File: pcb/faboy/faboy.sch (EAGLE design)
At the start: 51 parts, among them U1 MAX1595UMAX, U2 MCP73831, Y1 16MHZ

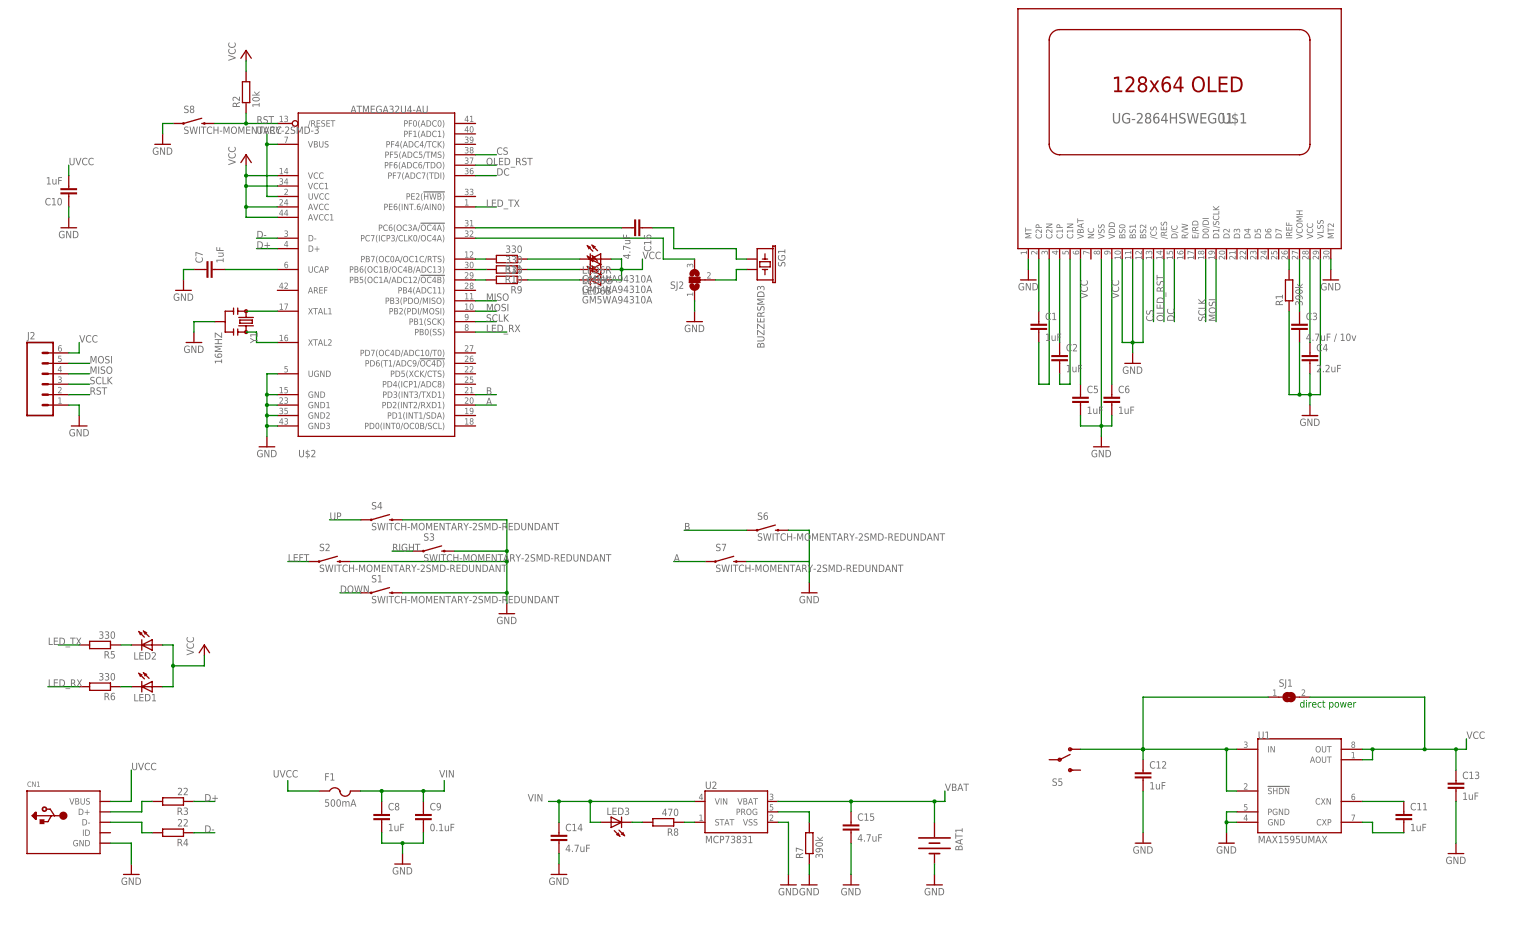
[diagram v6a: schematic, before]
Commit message: schematics > power path / pcb > only for 0.96 display
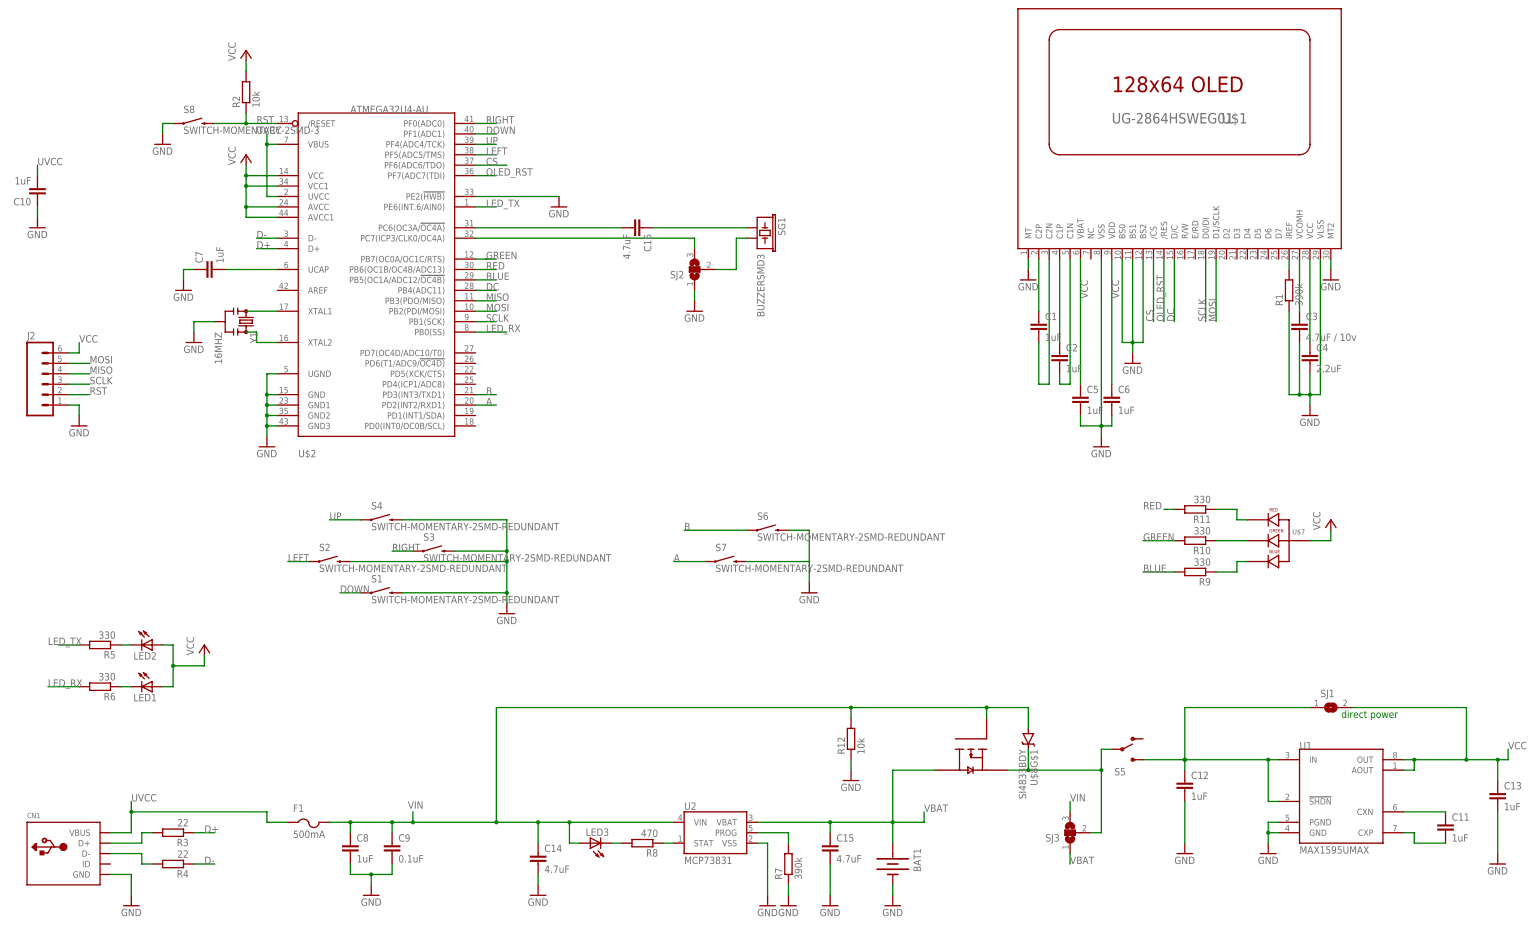
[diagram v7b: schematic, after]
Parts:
- removed LED6: GM5WA94310A, led:GM5WA94310A
- added R12: 10k, resistor:R-EU_R0805
- added SJ3: (no value), jumper:SJ2W
- added U$7: LED-RGB-P-LCC-4, SparkFun-LED:LED-RGB-P-LCC-4
- added U$8: SI4833BDY, SparkFun-DiscreteSemi:SI4833BDY
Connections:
- net N$6 renamed BLUE
- removed net N$29: R11.2, U$2.PB7(OC0A/OC1C/RTS)
- removed net N$30: LED6R.C, R11.1
- removed net N$31: LED6G.C, R10.1
- removed net N$32: LED6B.C, R9.1
- new net GREEN: R10.2, U$2.PB7(OC0A/OC1C/RTS)
- new net N$22: R10.1, U$7.GREEN_CATHODE
- new net N$24: R9.1, U$7.BLUE_CATHODE
- new net N$6: R11.1, U$7.RED_CATHODE
- new net RED: R11.2, U$2.PB6(OC1B/OC4B/ADC13)
- net CS: now also U$2.PF6(ADC6/TDO); no longer U$2.PF5(ADC5/TMS)
- net DC: now also U$2.PB4(ADC11); no longer U$2.PF7(ADC7(TDI)
- net DOWN: now also U$2.PF1(ADC1)
- net GND: now also R12.1, U$2.PE2(!HWB)
- net LEFT: now also U$2.PF5(ADC5/TMS)
- net N$10: now also S5.S; no longer S5.O
- net N$28: now also S5.P, SJ3.2, U$8G$1.C, U$8G$2.S2; no longer R10.2, U$2.PB6(OC1B/OC4B/ADC13)
- net OLED_RST: now also U$2.PF7(ADC7(TDI); no longer U$2.PF6(ADC6/TDO)
- net RIGHT: now also U$2.PF0(ADC0)
- net UP: now also U$2.PF4(ADC4/TCK)
- net VBAT: now also SJ3.1, U$8G$2.D2
- net VCC: now also U$7.ANODE; no longer LED6B.A, LED6G.A, LED6R.A
- net VIN: now also R12.2, SJ3.3, U$8G$1.A, U$8G$2.G2
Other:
- moved on the sheet: BAT1, C10, C11, C12, C13, C14, C15, C8, C9, CN1, F1, LED3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

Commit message: pcb > end of routing
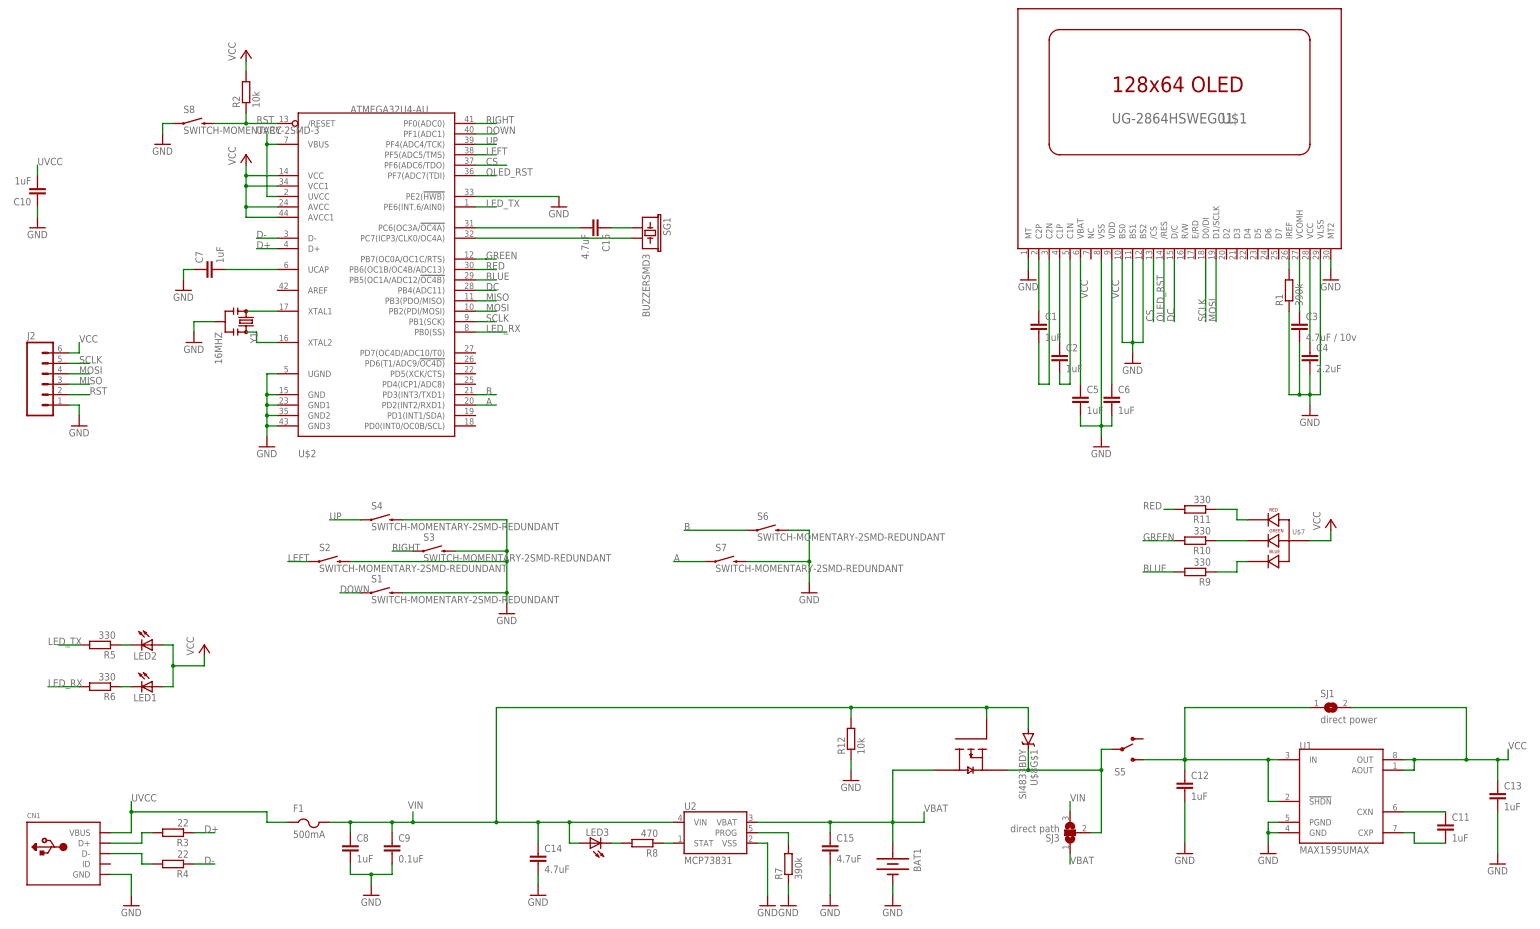
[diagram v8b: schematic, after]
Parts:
- removed SJ2: (no value), jumper:SJ2W
- SJ1: value (none) -> direct power
- SJ3: value (none) -> direct path
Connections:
- removed net N$27: SJ2.3, U$2.PC7(ICP3/CLK0/OC4A)
- net GND: no longer SJ2.1
- net MISO: now also J2.3; no longer J2.4
- net MOSI: now also J2.4; no longer J2.5
- net N$26: now also U$2.PC7(ICP3/CLK0/OC4A); no longer SJ2.2
- net SCLK: now also J2.5; no longer J2.3
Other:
- note removed: "direct power"
- moved on the sheet: C16, SG1
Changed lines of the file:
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@@
 <part name="GND17" library="supply1" deviceset="GND" device=""/>
 <part name="J2" library="SparkFun-Connectors" deviceset="M06" device="SMD-FEMALE-V2"/>
-<part name="SJ1" library="jumper" deviceset="SJ" device=""/>
+<part name="SJ1" library="jumper" deviceset="SJ" device="" value="direct power"/>
 <part name="U2" library="SparkFun-PowerIC" deviceset="MCP73831" device=""/>
 <part name="C14" library="resistor" deviceset="C-EU" device="C0805K" value="4.7uF"/>
@@
 <part name="GND22" library="supply1" deviceset="GND" device=""/>
 <part name="C16" library="resistor" deviceset="C-EU" device="C0805K" value="4.7uF"/>
-<part name="SJ2" library="jumper" deviceset="SJ2W" device=""/>
-<part name="GND23" library="supply1" deviceset="GND" device=""/>
 <part name="GND24" library="supply1" deviceset="GND" device=""/>
 <part name="R9" library="resistor" deviceset="R-EU_" device="R0805" value="330"/>
@@
 <part name="R12" library="resistor" deviceset="R-EU_" device="R0805" value="10k"/>
 <part name="GND26" library="supply1" deviceset="GND" device=""/>
-<part name="SJ3" library="jumper" deviceset="SJ2W" device=""/>
+<part name="SJ3" library="jumper" deviceset="SJ2W" device="" value="direct path"/>
 </parts>
 <sheets>
 <sheet>
 <plain>
-<text x="332.74" y="66.04" size="1.778" layer="91">direct power</text>
 </plain>
 <instances>
@@
 <instance part="GND13" gate="1" x="203.2" y="96.52"/>
 <instance part="BAT1" gate="G$1" x="223.52" y="30.48" rot="R270"/>
-<instance part="SG1" gate="G$1" x="190.5" y="185.42" rot="R270"/>
+<instance part="SG1" gate="G$1" x="162.56" y="185.42" rot="R270"/>
 <instance part="S5" gate="1" x="279.4" y="58.42"/>
 <instance part="S8" gate="G$1" x="53.34" y="210.82"/>
@@
 <instance part="GND21" gate="1" x="208.28" y="20.32"/>
 <instance part="GND22" gate="1" x="193.04" y="20.32"/>
-<instance part="C16" gate="G$1" x="162.56" y="185.42" rot="R270"/>
-<instance part="SJ2" gate="G$1" x="175.26" y="175.26" rot="R180"/>
-<instance part="GND23" gate="1" x="175.26" y="165.1"/>
+<instance part="C16" gate="G$1" x="152.4" y="185.42" rot="R270"/>
 <instance part="GND24" gate="1" x="25.4" y="137.16"/>
 <instance part="R9" gate="G$1" x="297.18" y="101.6" rot="R180"/>
@@
 <wire x1="187.96" y1="104.14" x2="203.2" y2="104.14" width="0.1524" layer="91"/>
 <wire x1="203.2" y1="104.14" x2="203.2" y2="101.6" width="0.1524" layer="91"/>
+<junction x="203.2" y="104.14"/>
 </segment>
 <segment>
@@
 <pinref part="GND17" gate="1" pin="GND"/>
 <wire x1="223.52" y1="25.4" x2="223.52" y2="22.86" width="0.1524" layer="91"/>
-</segment>
-<segment>
-<pinref part="GND23" gate="1" pin="GND"/>
-<pinref part="SJ2" gate="G$1" pin="1"/>
-<wire x1="175.26" y1="167.64" x2="175.26" y2="170.18" width="0.1524" layer="91"/>
 </segment>
 <segment>
@@
 </segment>
 <segment>
-<pinref part="J2" gate="G$1" pin="5"/>
-<wire x1="22.86" y1="152.4" x2="27.94" y2="152.4" width="0.1524" layer="91"/>
-<label x="27.94" y="152.4" size="1.778" layer="95"/>
+<pinref part="J2" gate="G$1" pin="4"/>
+<wire x1="22.86" y1="149.86" x2="27.94" y2="149.86" width="0.1524" layer="91"/>
+<label x="25.4" y="149.86" size="1.778" layer="95"/>
 </segment>
 </net>
@@
 </segment>
 <segment>
-<pinref part="J2" gate="G$1" pin="4"/>
-<wire x1="22.86" y1="149.86" x2="27.94" y2="149.86" width="0.1524" layer="91"/>
-<label x="27.94" y="149.86" size="1.778" layer="95"/>
+<pinref part="J2" gate="G$1" pin="3"/>
+<wire x1="22.86" y1="147.32" x2="27.94" y2="147.32" width="0.1524" layer="91"/>
+<label x="25.4" y="147.32" size="1.778" layer="95"/>
 </segment>
 </net>
@@
 <pinref part="U$2" gate="G$1" pin="PC6(OC3A/!OC4A)"/>
 <pinref part="C16" gate="G$1" pin="2"/>
-<wire x1="121.92" y1="185.42" x2="157.48" y2="185.42" width="0.1524" layer="91"/>
+<wire x1="121.92" y1="185.42" x2="147.32" y2="185.42" width="0.1524" layer="91"/>
 </segment>
 </net>
@@
 <segment>
 <pinref part="SG1" gate="G$1" pin="1"/>
-<wire x1="187.96" y1="185.42" x2="165.1" y2="185.42" width="0.1524" layer="91"/>
+<wire x1="160.02" y1="185.42" x2="154.94" y2="185.42" width="0.1524" layer="91"/>
 <pinref part="C16" gate="G$1" pin="1"/>
 </segment>
@@
 <net name="N$26" class="0">
 <segment>
-<wire x1="185.42" y1="175.26" x2="185.42" y2="182.88" width="0.1524" layer="91"/>
 <pinref part="SG1" gate="G$1" pin="2"/>
-<wire x1="185.42" y1="182.88" x2="187.96" y2="182.88" width="0.1524" layer="91"/>
-<pinref part="SJ2" gate="G$1" pin="2"/>
-<wire x1="180.34" y1="175.26" x2="185.42" y2="175.26" width="0.1524" layer="91"/>
-</segment>
-</net>
-<net name="N$27" class="0">
-<segment>
 <pinref part="U$2" gate="G$1" pin="PC7(ICP3/CLK0/OC4A)"/>
-<wire x1="121.92" y1="182.88" x2="175.26" y2="182.88" width="0.1524" layer="91"/>
-<pinref part="SJ2" gate="G$1" pin="3"/>
-<wire x1="175.26" y1="182.88" x2="175.26" y2="180.34" width="0.1524" layer="91"/>
+<wire x1="121.92" y1="182.88" x2="160.02" y2="182.88" width="0.1524" layer="91"/>
 </segment>
 </net>
 <net name="SCLK" class="0">
-<segment>
-<pinref part="J2" gate="G$1" pin="3"/>
-<wire x1="22.86" y1="147.32" x2="27.94" y2="147.32" width="0.1524" layer="91"/>
-<label x="27.94" y="147.32" size="1.778" layer="95"/>
-</segment>
 <segment>
 <pinref part="U$1" gate="G$1" pin="D0/DI"/>
@@
 <label x="124.46" y="162.56" size="1.778" layer="95"/>
 </segment>
-</net>
+<segment>
+<pinref part="J2" gate="G$1" pin="5"/>
+<wire x1="22.86" y1="152.4" x2="27.94" y2="152.4" width="0.1524" layer="91"/>
+<label x="25.4" y="152.4" size="1.778" layer="95"/>
+</segment>
+</net>
